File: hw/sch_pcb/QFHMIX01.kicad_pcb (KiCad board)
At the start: 2 copper layers, 90.9 x 90.9 mm, 215 parts, among them J1 HEADER_1x08, J2 +9V, M1 HOLE, M2 HOLE, M3 HOLE, M4 HOLE, M5 HOLE, M6 HOLE, M7 HOLE, M8 HOLE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

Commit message: Edit PCB
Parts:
- moved L60 150.4 mm to (153.4, 72.8), turned to -45 degrees
- moved L39 149.7 mm to (156.1, 75.2), turned to -45 degrees
- moved L61 146.7 mm to (157.0, 67.7), turned to 180 degrees
- moved L65 146.5 mm to (160.0, 68.2), turned to 90 degrees
- moved C30 138.2 mm to (162.6, 74.2)
- moved L63 12.9 mm to (161.8, 71.9)
- moved C29 10.9 mm to (161.0, 80.8)
- moved L69 9.80 mm to (158.9, 78.0), turned to -45 degrees
- moved C65 8.62 mm to (159.4, 74.5), turned to -135 degrees
- moved L59 8.52 mm to (153.4, 67.8)
- moved L58 8.39 mm to (150.7, 70.2)
- moved C58 8.30 mm to (152.8, 69.7)
- moved L67 7.48 mm to (160.4, 75.7), turned to 45 degrees
- moved L30 7.14 mm to (153.5, 70.2)
- moved C63 5.31 mm to (156.1, 71.5)
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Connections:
- C72 pad 2: (no net) -> Net-(C72-Pad2)
- U11 pad 6: (no net) -> Net-(C72-Pad2)
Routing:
- net Net-(R13-Pad2): track 0.00 -> 79.5 mm
- net /CLK_MIX1_P: track 81.1 -> 1.57 mm
- net VCC: track 140.8 -> 68.5 mm, vias 5 -> 3
- net CLK_IN_N: track 0.00 -> 72.3 mm, vias 0 -> 2
- net GND: track 85.3 -> 67.6 mm, vias 379 -> 374
- net DEM_OUTB_P: track 17.1 -> 8.46 mm
- net DEM_OUTA_N: track 0.00 -> 8.59 mm
- net Net-(C22-Pad2): track 7.97 -> 0.00 mm, vias 1 -> 0
- net DEM_OUTB_N: track 15.4 -> 7.83 mm
- net DEM_OUTA_P: track 0.00 -> 7.53 mm
- net Net-(C63-Pad1): track 7.25 -> 0.00 mm
- net +5V: track 176.6 -> 182.5 mm, vias 22 -> 21
- net Net-(C63-Pad2): track 5.70 -> 0.00 mm
- net Net-(C55-Pad1): track 0.00 -> 4.41 mm
- net Net-(C57-Pad2): track 6.08 -> 1.67 mm
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
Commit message: Edit PCB
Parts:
- moved C48 73.6 mm to (220.8, 113.1)
- moved C51 73.6 mm to (232.4, 110.0)
- moved C53 73.6 mm to (247.7, 113.1)
- moved C54 73.6 mm to (248.3, 107.4)
- moved C55 73.6 mm to (221.5, 107.4)
- moved L16 73.6 mm to (207.9, 111.8)
- moved L32 73.6 mm to (236.6, 113.1)
- moved L33 73.6 mm to (215.9, 110.1)
- moved L34 73.6 mm to (217.2, 107.4)
- moved L35 73.6 mm to (239.4, 110.1)
- moved L37 73.6 mm to (240.7, 107.4)
- moved L38 73.6 mm to (240.5, 113.1)
- moved L62 73.6 mm to (211.5, 109.9)
- moved L66 73.6 mm to (243.2, 110.1)
- moved L70 73.6 mm to (244.3, 113.1)
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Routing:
- net Net-(C65-Pad1): track 3.81 -> 0.00 mm
- net Net-(C65-Pad2): track 3.79 -> 0.00 mm
- net (no net): track 35.0 -> 32.3 mm
- net Net-(C30-Pad1): track 2.09 -> 0.00 mm
- net Net-(C29-Pad1): track 2.03 -> 0.00 mm
- net GND: track 67.6 -> 65.7 mm

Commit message: Edit PCB
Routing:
- net (no net): track 32.3 -> 6.17 mm
- net Net-(C37-Pad1): track 10.7 -> 3.61 mm
- net Net-(C38-Pad1): track 10.7 -> 3.69 mm
- net Net-(C34-Pad1): track 4.03 -> 0.00 mm
- net Net-(C46-Pad2): track 4.01 -> 0.00 mm
- net Net-(C33-Pad1): track 3.22 -> 0.00 mm
- net Net-(C45-Pad2): track 3.11 -> 0.00 mm
- net GND: track 65.7 -> 63.9 mm, vias 374 -> 372
- net Net-(C56-Pad2): track 6.06 -> 4.38 mm
- net Net-(C57-Pad2): track 1.67 -> 0.00 mm

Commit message: Edit PCB
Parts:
- removed C71, C81: 100nF, Capacitor_SMD:C_0603_1608Metric
- removed C73, C75: 10uF/16, Capacitor_SMD:C_0805_2012Metric
- removed C77, C79: 47uF/6,3V, Capacitor_SMD:C_0805_2012Metric
- removed D2: RED, Mlab_D:LED_1206
- removed L50: BLM21PG331SN1D, Mlab_R:SMD-0805
- removed R47: 10k, Resistor_SMD:R_0603_1608Metric
- removed R51: 45k3, Resistor_SMD:R_0603_1608Metric
- removed R53: 240R, Resistor_SMD:R_0603_1608Metric
- removed U10: TPS563249, Package_TO_SOT_SMD:SOT-23-6
- added C66: 100nF, Mlab_C:SMD-0603, F.Cu at (228.5, 144.9)
- added U1: LM1117MP-3,3/NO, Package_TO_SOT_SMD:SOT-223-3_TabPin2, F.Cu at (231.2, 156.0)
- C67: value 10uF/16 -> 100nF; footprint Capacitor_SMD:C_0805_2012Metric -> Mlab_C:SMD-0603; moved to F.Cu
- C69: value 100nF -> 10uF; footprint Capacitor_SMD:C_0603_1608Metric -> Capacitor_SMD:C_0805_2012Metric; moved to F.Cu
- L48: value 1u5H - ETQ-P3M1R5KVP -> BLM21PG331SN1D; footprint Mlab_L:PCC-M0530M-LP -> Mlab_L:SMD-0805; moved to F.Cu
- R4, R5, R7, R8: value 68 -> 68R
- moved C69 141.1 mm to (238.4, 153.4)
- moved C67 134.5 mm to (232.7, 142.2)
- moved L48 121.7 mm to (228.9, 142.4)
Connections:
- C67 pad 2: VCC -> Net-(C67-Pad2)
- C69 pad 1: GND -> Net-(C67-Pad2)
- C69 pad 2: VCC -> GND
- L48 pad 1: Net-(C71-Pad1) -> Net-(C67-Pad2)
- L48 pad 2: Net-(C73-Pad2) -> +3V3
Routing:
- net CLK_IN_P: track 0.00 -> 74.2 mm, vias 0 -> 2
- net Net-(C1-Pad2): track 79.5 -> 5.31 mm, vias 2 -> 0

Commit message: Rotate connection block.
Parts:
- turned J1 to -45 degrees
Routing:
- net GND: vias 372 -> 371
- net DEM_OUTA_P: vias 0 -> 1
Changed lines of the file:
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@@
-(kicad_pcb (version 20210228) (generator pcbnew)
+(kicad_pcb (version 20210606) (generator pcbnew)
   (general
     (thickness 1.6)
@@
   (net 140 "Net-(C72-Pad2)")
   (footprint "Mlab_CON:IDC381-8-110" (layer "F.Cu")
-    (at 120.5 119.5 135)
+    (at 120.5 119.5 -45)
     (property "Sheetfile" "QFHMIX01.kicad_sch")
     (property "Sheetname" "")
@@
     (fp_line (start 16.002 4.191) (end -16.002 4.191) (layer "F.Fab") (width 0.1))
     (fp_line (start -16.002 4.191) (end -16.002 -4.191) (layer "F.Fab") (width 0.1))
-    (pad "" np_thru_hole circle locked (at -11.43 -3.2 135) (size 1.6 1.6) (drill 1.6) (layers *.Cu *.Mask))
-    (pad "" np_thru_hole circle locked (at 7.62 3.2 135) (size 1.6 1.6) (drill 1.6) (layers *.Cu *.Mask))
-    (pad "" np_thru_hole circle locked (at 11.43 -3.2 135) (size 1.6 1.6) (drill 1.6) (layers *.Cu *.Mask))
-    (pad "" np_thru_hole circle locked (at 3.81 -3.2 135) (size 1.6 1.6) (drill 1.6) (layers *.Cu *.Mask))
-    (pad "" np_thru_hole circle locked (at -3.81 -3.2 135) (size 1.6 1.6) (drill 1.6) (layers *.Cu *.Mask))
-    (pad "" np_thru_hole circle locked (at -7.62 3.2 135) (size 1.6 1.6) (drill 1.6) (layers *.Cu *.Mask))
-    (pad "1" thru_hole circle locked (at -13.335 0 135) (size 2.5 2.5) (drill 1.4) (layers *.Cu *.Mask)
+    (pad "" np_thru_hole circle locked (at -11.43 -3.2 315) (size 1.6 1.6) (drill 1.6) (layers *.Cu *.Mask))
+    (pad "" np_thru_hole circle locked (at 7.62 3.2 315) (size 1.6 1.6) (drill 1.6) (layers *.Cu *.Mask))
+    (pad "" np_thru_hole circle locked (at 11.43 -3.2 315) (size 1.6 1.6) (drill 1.6) (layers *.Cu *.Mask))
+    (pad "" np_thru_hole circle locked (at 3.81 -3.2 315) (size 1.6 1.6) (drill 1.6) (layers *.Cu *.Mask))
+    (pad "" np_thru_hole circle locked (at -3.81 -3.2 315) (size 1.6 1.6) (drill 1.6) (layers *.Cu *.Mask))
+    (pad "" np_thru_hole circle locked (at -7.62 3.2 315) (size 1.6 1.6) (drill 1.6) (layers *.Cu *.Mask))
+    (pad "1" thru_hole circle locked (at -13.335 0 315) (size 2.5 2.5) (drill 1.4) (layers *.Cu *.Mask)
       (net 63 "CLK_IN_N") (pintype "input"))
-    (pad "2" thru_hole circle locked (at -9.525 0 135) (size 2.5 2.5) (drill 1.4) (layers *.Cu *.Mask)
+    (pad "2" thru_hole circle locked (at -9.525 0 315) (size 2.5 2.5) (drill 1.4) (layers *.Cu *.Mask)
       (net 62 "CLK_IN_P") (pintype "input"))
-    (pad "3" thru_hole circle locked (at -5.715 0 135) (size 2.5 2.5) (drill 1.4) (layers *.Cu *.Mask)
+    (pad "3" thru_hole circle locked (at -5.715 0 315) (size 2.5 2.5) (drill 1.4) (layers *.Cu *.Mask)
       (net 60 "DEM_OUTA_N") (pintype "input"))
-    (pad "4" thru_hole circle locked (at -1.904999 0 135) (size 2.5 2.5) (drill 1.4) (layers *.Cu *.Mask)
+    (pad "4" thru_hole circle locked (at -1.904999 0 315) (size 2.5 2.5) (drill 1.4) (layers *.Cu *.Mask)
       (net 59 "DEM_OUTA_P") (pintype "input"))
-    (pad "5" thru_hole circle locked (at 1.904999 0 135) (size 2.5 2.5) (drill 1.4) (layers *.Cu *.Mask)
+    (pad "5" thru_hole circle locked (at 1.904999 0 315) (size 2.5 2.5) (drill 1.4) (layers *.Cu *.Mask)
       (net 64 "DEM_OUTB_N") (pintype "input"))
-    (pad "6" thru_hole circle locked (at 5.715 0 135) (size 2.5 2.5) (drill 1.4) (layers *.Cu *.Mask)
+    (pad "6" thru_hole circle locked (at 5.715 0 315) (size 2.5 2.5) (drill 1.4) (layers *.Cu *.Mask)
       (net 61 "DEM_OUTB_P") (pintype "input"))
-    (pad "7" thru_hole circle locked (at 9.525 0 135) (size 2.5 2.5) (drill 1.4) (layers *.Cu *.Mask)
+    (pad "7" thru_hole circle locked (at 9.525 0 315) (size 2.5 2.5) (drill 1.4) (layers *.Cu *.Mask)
       (net 1 "GND") (pintype "input"))
-    (pad "8" thru_hole circle locked (at 13.335 0 135) (size 2.5 2.5) (drill 1.4) (layers *.Cu *.Mask)
+    (pad "8" thru_hole circle locked (at 13.335 0 315) (size 2.5 2.5) (drill 1.4) (layers *.Cu *.Mask)
       (net 2 "VCC") (pintype "input"))
     (model "${KISYS3DMOD}/Connector_PinSocket_2.54mm.3dshapes/PinSocket_1x08_P2.54mm_Vertical.wrl"
@@
     (effects (font (size 1.5 1.5) (thickness 0.3)))
   )
-  (gr_text "GND" (at 168.4 106.8 45) (layer "F.SilkS")
-    (effects (font (size 1.5 1.5) (thickness 0.3)))
-  )
   (gr_text "GND" (at 132.25 121.75 45) (layer "F.SilkS")
     (effects (font (size 1.5 1.5) (thickness 0.3)))
@@
     (effects (font (size 1.5 1.5) (thickness 0.2)))
   )
+  (gr_text "GND" (at 168.4 106.8 45) (layer "F.SilkS")
+    (effects (font (size 1.5 1.5) (thickness 0.3)))
+  )
   (gr_text "LOOP_A+" (at 150.3 131.5) (layer "F.SilkS")
     (effects (font (size 1.5 1.5) (thickness 0.2)))
@@
   (via (at 137.2 105.5) (size 0.75) (drill 0.4) (layers "F.Cu" "B.Cu") (net 1))
   (via (at 149.8 113.4) (size 0.75) (drill 0.4) (layers "F.Cu" "B.Cu") (net 1))
-  (via (at 122 118) (size 0.75) (drill 0.4) (layers "F.Cu" "B.Cu") (net 1))
   (via (at 121.725 69.325) (size 0.75) (drill 0.4) (layers "F.Cu" "B.Cu") (net 1))
   (via (at 115.975 69.6) (size 0.75) (drill 0.4) (layers "F.Cu" "B.Cu") (net 1))
@@
   (segment (start 128.132621 73.845492) (end 127.260716 72.973587) (width 0.3) (layer "B.Cu") (net 52))
   (segment (start 127.260716 72.973587) (end 127.260716 72.832165) (width 0.3) (layer "B.Cu") (net 52))
+  (via (at 122 118) (size 0.75) (drill 0.4) (layers "F.Cu" "B.Cu") (net 59))
   (segment (start 119.175704 118.294224) (end 118.982659 118.294224) (width 0.5) (layer "B.Cu") (net 59))
   (segment (start 124.340998 112.796632) (end 123.248815 113.888815) (width 0.5) (layer "B.Cu") (net 59))

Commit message: Edit PCB
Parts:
- C66, C67, C69, L48, U1: moved to B.Cu
- moved C70 126.1 mm to (226.6, 104.9)
- moved C72 126.1 mm to (223.1, 104.9)
- moved C74 126.1 mm to (220.3, 113.3)
- moved C76 126.1 mm to (220.3, 110.3)
- moved C78 126.1 mm to (207.6, 111.2)
- moved C82 126.1 mm to (227.3, 108.0)
- moved L49 126.1 mm to (222.7, 121.9)
- moved U11 126.1 mm to (210.2, 106.7)
- moved D3 126.1 mm to (204.5, 107.0)
- moved C68 126.1 mm to (236.4, 123.0)
- moved C80 126.1 mm to (237.1, 127.5)
- moved L51 126.1 mm to (219.3, 107.5)
- moved R48 126.1 mm to (245.6, 127.7)
- moved R52 126.1 mm to (224.6, 110.5)
- moved R54 126.1 mm to (228.8, 110.5)
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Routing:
- net Net-(R13-Pad2): track 79.5 -> 3.68 mm
- net Net-(C4-Pad1): track 46.9 -> 0.00 mm, vias 2 -> 1
- net +5V: track 182.5 -> 136.5 mm, vias 21 -> 15
- net /CLK_MIX2_N: track 0.00 -> 40.2 mm, vias 0 -> 2
- net Net-(C58-Pad1): track 15.6 -> 0.00 mm, vias 2 -> 0
- net GND: track 63.9 -> 49.2 mm, vias 371 -> 313
- net Net-(C57-Pad1): track 9.14 -> 0.00 mm, vias 7 -> 0
- net Net-(C7-Pad1): track 6.75 -> 0.00 mm, vias 1 -> 0
- net Net-(C5-Pad1): track 6.56 -> 0.00 mm
- net Net-(C6-Pad1): track 6.51 -> 0.00 mm
- net (no net): track 6.17 -> 0.00 mm
- net Net-(C22-Pad2): track 0.00 -> 4.76 mm
- net Net-(L1-Pad1): track 4.54 -> 0.00 mm, vias 7 -> 0
- net Net-(C55-Pad1): track 4.41 -> 0.00 mm
- net Net-(C56-Pad2): track 4.38 -> 0.00 mm
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- removed copper zone on B.Cu, net Net-(C53-Pad1)
- removed copper zone on F.Cu, net Net-(C53-Pad1)
- removed copper zone on B.Cu, net Net-(C57-Pad1)
- removed copper zone on F.Cu, net Net-(C57-Pad1)
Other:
- board text removed: "LOOP_A+"

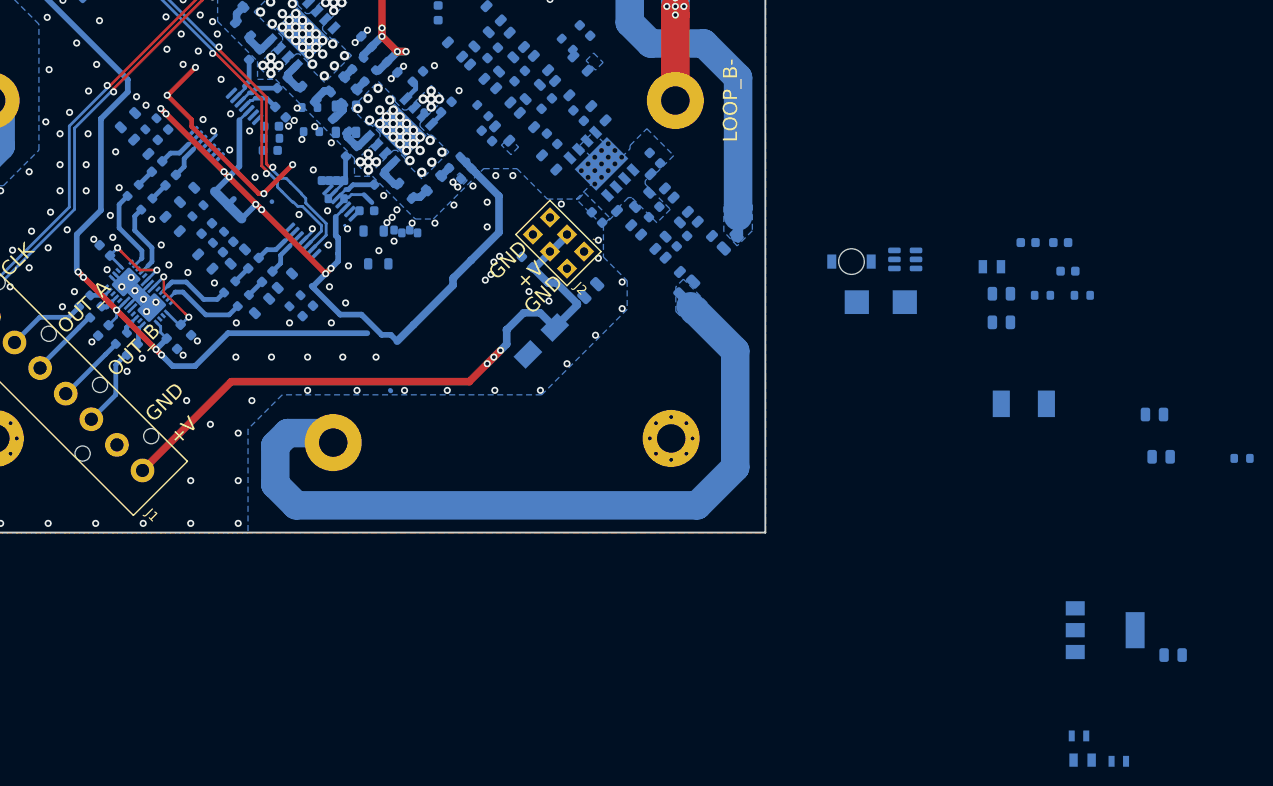
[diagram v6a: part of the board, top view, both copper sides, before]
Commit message: Improve components placement.
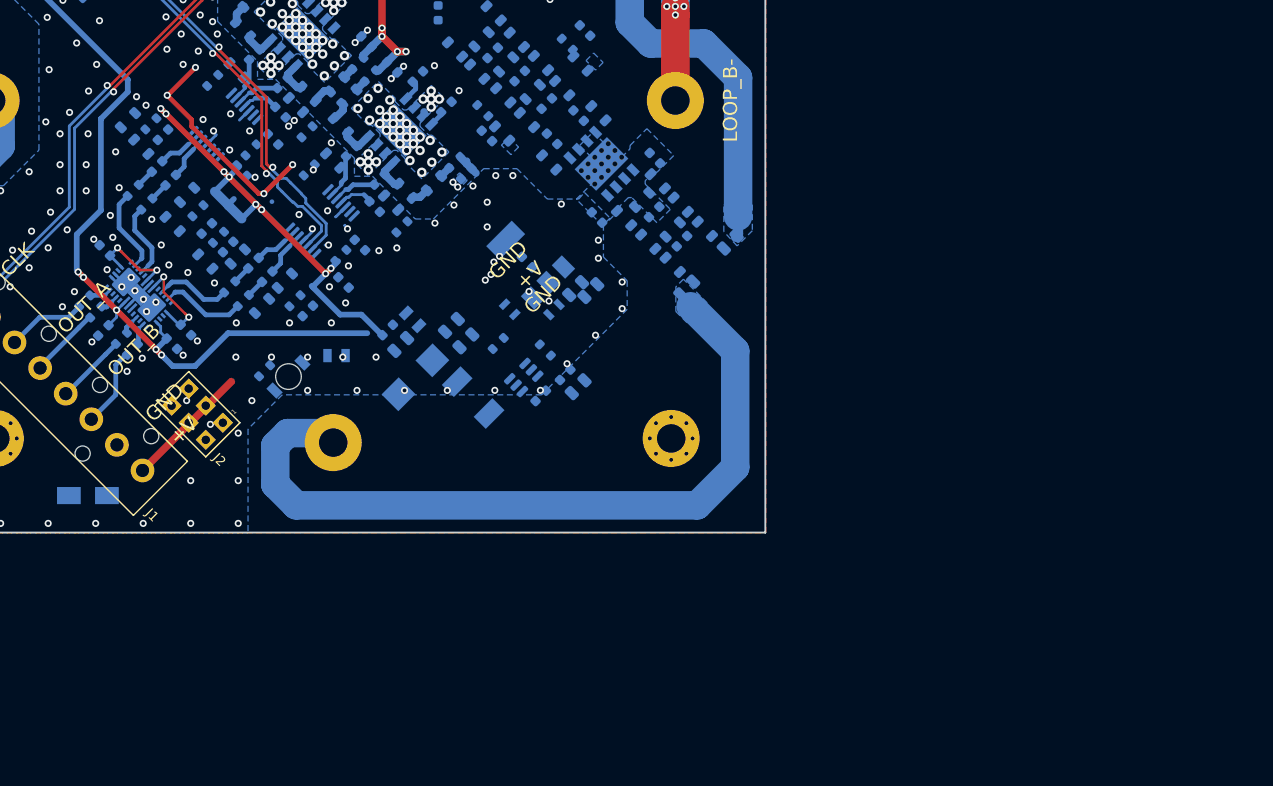
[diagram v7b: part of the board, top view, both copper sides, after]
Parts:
- moved L48 89.3 mm to (150.3, 116.8), turned to 180 degrees
- moved R54 86.4 mm to (142.8, 118.4), turned to -135 degrees
- moved C80 80.9 mm to (157.1, 115.7), turned to 45 degrees
- moved C67 76.1 mm to (173.2, 112.0), turned to 45 degrees
- moved C66 74.9 mm to (168.6, 112.0), turned to 135 degrees
- moved R48 74.2 mm to (172.3, 116.3), turned to 135 degrees
- moved C69 73.8 mm to (175.5, 109.8), turned to 45 degrees
- moved U1 72.2 mm to (170.4, 106.9), turned to 135 degrees
- moved C82 71.9 mm to (155.7, 114.1), turned to 45 degrees
- moved L51 61.2 mm to (158.3, 113.0), turned to 135 degrees
- moved C68 60.7 mm to (175.8, 120.1), turned to -135 degrees
- moved D3 60.5 mm to (145.3, 119.0), turned to 45 degrees
- moved L49 58.0 mm to (164.7, 121.3), turned to -45 degrees
- moved C74 57.9 mm to (162.4, 113.7), turned to -135 degrees
- moved R52 57.5 mm to (167.4, 115.6), turned to 45 degrees
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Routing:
- net VCC: track 68.5 -> 13.2 mm, vias 3 -> 1
- net +5V: track 136.5 -> 99.1 mm, vias 15 -> 18
- net GND: track 49.2 -> 44.7 mm, vias 313 -> 298
- net /LNA/LNA_OUT_2_P: track 0.00 -> 4.52 mm
- net Net-(C13-Pad1): track 0.00 -> 4.04 mm
- net Net-(C11-Pad1): track 4.04 -> 1.38 mm
- net Net-(C10-Pad1): track 0.00 -> 1.35 mm
- net Net-(L4-Pad1): vias 1 -> 0
- net Net-(L2-Pad1): vias 1 -> 0
- net Net-(C74-Pad2): vias 0 -> 1
- net Net-(C72-Pad2): vias 0 -> 1
- net Net-(C67-Pad2): vias 0 -> 2

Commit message: Layout improvement.
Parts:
- moved L48 8.88 mm to (141.6, 115.4)
- moved C12 7.47 mm to (137.4, 88.9), turned to 45 degrees
- moved C27 5.82 mm to (175.5, 104.4)
- moved C28 5.54 mm to (174.1, 102.9), turned to 45 degrees
- moved C18 3.96 mm to (137.5, 99.6), turned to 45 degrees
- moved L8 3.59 mm to (129.7, 95.4), turned to 45 degrees
- moved L11 3.54 mm to (139.9, 105.7), turned to 45 degrees
- moved C15 3.30 mm to (140.7, 102.6), turned to 45 degrees
- moved R24 3.17 mm to (128.4, 94.5)
- moved L4 3.10 mm to (143.0, 89.9)
- moved L10 3.09 mm to (142.5, 104.7), turned to -45 degrees
- moved L12 3.03 mm to (134.4, 100.3), turned to 45 degrees
- moved L1 2.77 mm to (153.4, 100.0)
- moved L9 2.74 mm to (132.5, 94.5)
- moved C13 2.61 mm to (153.7, 103.7)
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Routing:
- net /CLK_MIX1_P: track 0.05 -> 24.6 mm
- net /CLK_MIX1_N: track 0.02 -> 24.2 mm
- net +3V3: track 100.2 -> 85.5 mm
- net Net-(C10-Pad1): track 1.35 -> 6.94 mm
- net Net-(C11-Pad1): track 1.38 -> 6.80 mm
- net GND: track 44.7 -> 48.9 mm, vias 298 -> 296
- net +5V: track 99.1 -> 95.5 mm
- net Net-(C13-Pad1): track 4.04 -> 7.07 mm
- net Net-(L2-Pad1): track 0.00 -> 2.06 mm
- net Net-(L12-Pad1): track 0.00 -> 1.84 mm
- net Net-(L7-Pad1): track 0.00 -> 1.77 mm
- net Net-(L6-Pad1): track 0.00 -> 1.76 mm
- net Net-(L8-Pad2): track 0.00 -> 1.71 mm
- net Net-(L12-Pad2): track 0.00 -> 1.69 mm
- net Net-(L4-Pad1): track 0.00 -> 1.62 mm
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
